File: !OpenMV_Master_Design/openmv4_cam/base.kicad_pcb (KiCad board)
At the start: 4 copper layers, 129.6 x 57.7 mm, 58 parts, among them J5 XF2M-1015-1A, Q1 BSS138, Q2 Si2301BDS, U1 STM32H743VIT6, U2 OV7725, U5 TPS731XX, U8 PAM2305AABADJ, X1 MF-CON-MICROUSB-RIGHT, X2 USD-1040310811, Y1 7S-12.000MAHE-T

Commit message: Moved SD card
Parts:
- moved X2 16.6 mm to (149.5, 90.3), turned to 0 degrees
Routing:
- net /SDIO_CMD: track 22.1 -> 11.1 mm
- net /SDIO_CLK: track 16.4 -> 6.95 mm
- net /SDIO_D3: track 18.3 -> 11.0 mm
- net /SDIO_D2: track 17.4 -> 11.8 mm
- net GND: track 75.9 -> 72.8 mm, vias 36 -> 35
- net VCC: vias 32 -> 30
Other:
- board size 129.6 x 57.7 mm -> 35.8 x 44.4 mm
- board text removed: "3.3V"
- board text removed: "BOOT"
- board text removed: "Built by MacroFab"
- board text removed: "LED1=Red"
- board text removed: "LED2=Green"
- board text removed: "LED3=Blue"
- board text removed: "LED4=IR"
- board text removed: "Made in USA"
- board text removed: "P0"
- board text removed: "P1"
- board text removed: "P2"
- board text removed: "P3"
- board text removed: "P4"
- board text removed: "P5"
- board text removed: "P6"
- board text removed: "P7"
- board text removed: "P8"
- board text removed: "P9"
- board text removed: "SYN"
- board text removed: "VIN"
- board text removed: "v00"

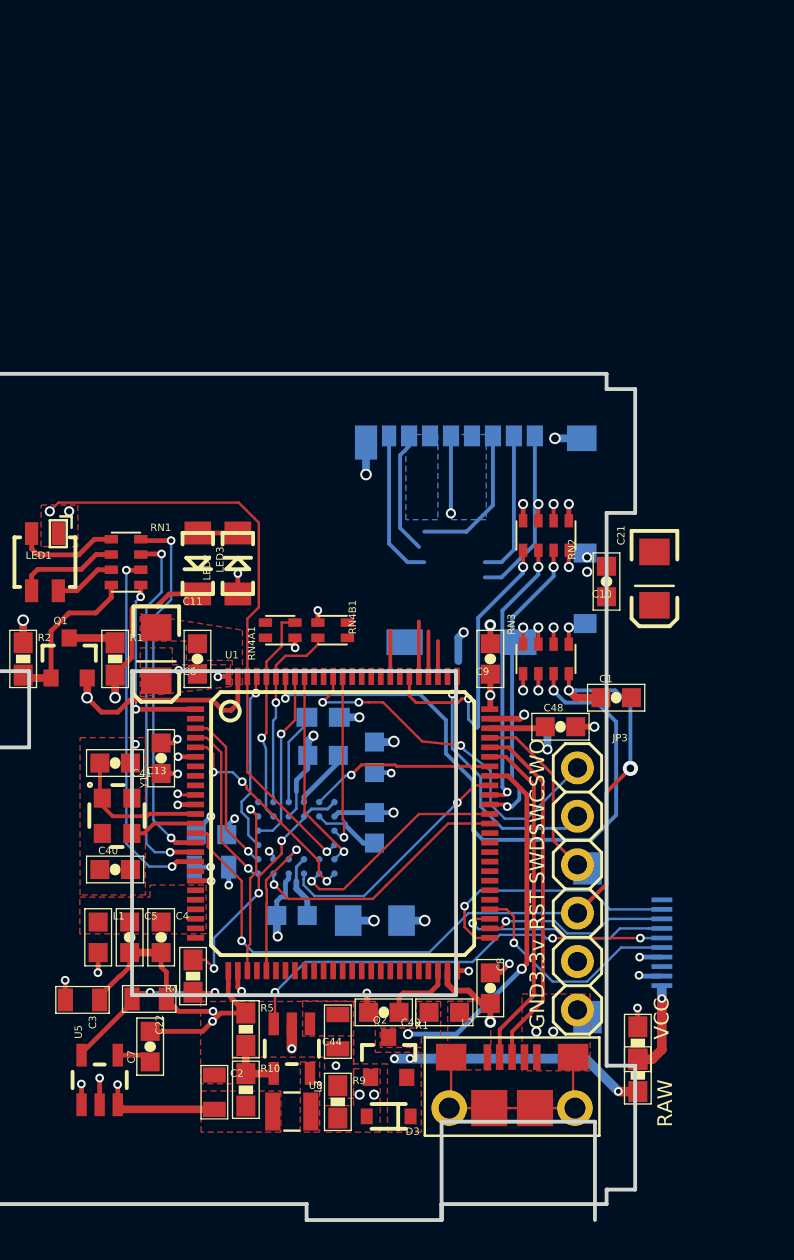
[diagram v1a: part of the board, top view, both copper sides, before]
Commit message: Move USB to cam side, more SD card changes
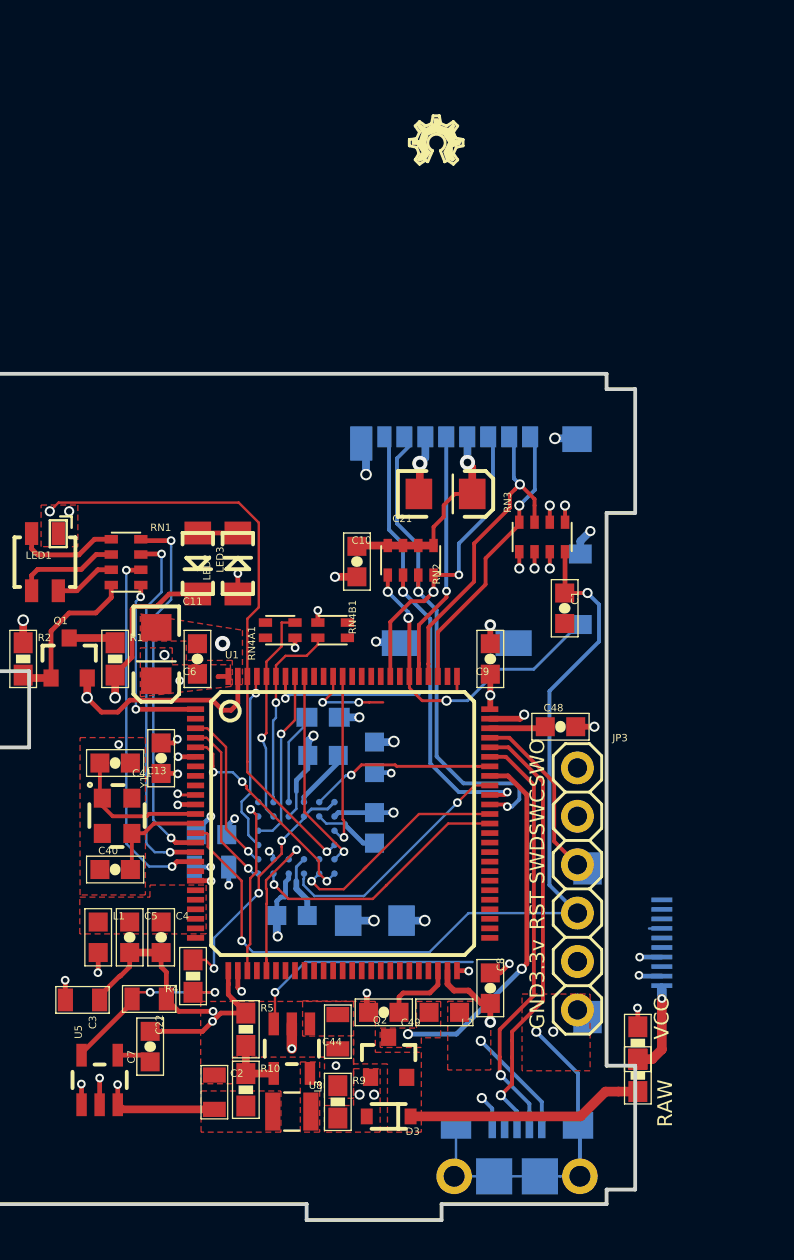
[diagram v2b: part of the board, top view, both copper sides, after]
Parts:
- added LOGO1: OSHW_LOGO_FILLX0100-NT, base:OSHW_FILLX100_NOTEXT, F.Cu at (152.0, 76.2)
- J5: footprint XF2M-1015-1A:XF2M-1015-1A -> base:XF2M-1015-1A
- X1: moved to B.Cu
- moved C10 13.1 mm to (149.2, 97.1), turned to 270 degrees
- moved C21 11.8 mm to (153.9, 93.5), turned to 0 degrees
- moved RN2 7.22 mm to (152.1, 97.0)
- moved RN3 6.40 mm to (159.0, 95.8)
- moved C1 5.41 mm to (160.2, 99.5), turned to 270 degrees
- moved X1 3.59 mm to (157.7, 128.0), turned to 180 degrees
- moved X2 0.25 mm to (149.2, 90.3)
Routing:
- net /BOOT0: track 34.6 -> 9.16 mm
- net /SPI3_SCLK/TRACESWO: track 19.5 -> 4.76 mm, vias 3 -> 2
- net /SPI2_NSS: track 13.8 -> 0.00 mm, vias 1 -> 0
- net /SWCLK: track 13.4 -> 0.67 mm, vias 1 -> 0
- net /SPI2_MOSI: track 12.1 -> 0.00 mm, vias 1 -> 0
- net /SPI2_MISO: track 11.5 -> 0.68 mm, vias 1 -> 0
- net /PWR_EN: track 23.3 -> 12.7 mm, vias 3 -> 1
- net /SPI2_SCLK: track 9.83 -> 0.00 mm, vias 1 -> 0
- net VCC: track 32.0 -> 39.7 mm, vias 30 -> 27
- net /SDIO_CLK: track 6.95 -> 13.2 mm
- net GND: track 72.8 -> 78.9 mm, vias 35 -> 36
- net /SDIO_D3: track 11.0 -> 17.0 mm
- net Net-(X1-PadS1): track 12.0 -> 17.9 mm, vias 0 -> 1
- net Net-(L2-Pad1): track 0.00 -> 5.76 mm, vias 0 -> 1
- net /SDIO_CMD: track 11.1 -> 16.2 mm, vias 1 -> 2
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- removed copper zone on B.Cu, net GND
- removed copper zone on B.Cu, net VCC
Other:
- outline, holes or cut-outs redrawn

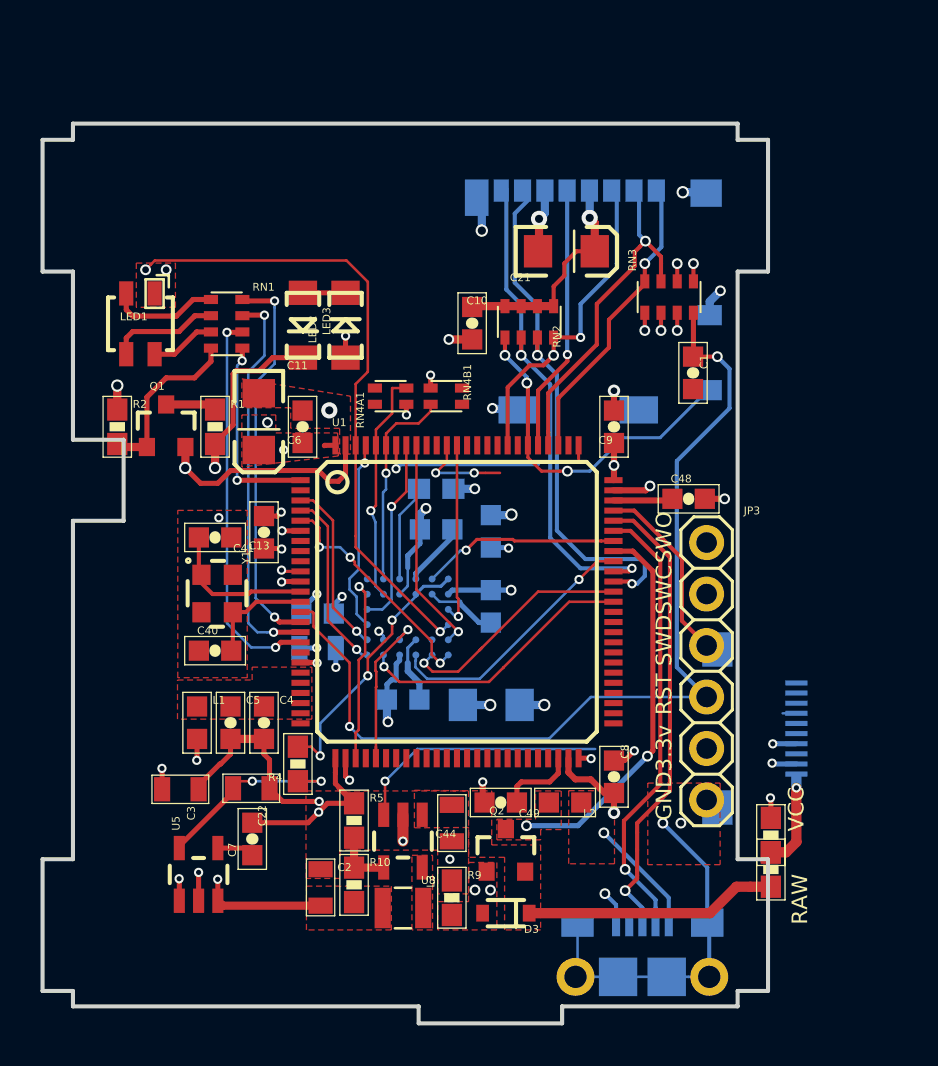
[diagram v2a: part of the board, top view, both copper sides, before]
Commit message: Fixed connections to debug headers
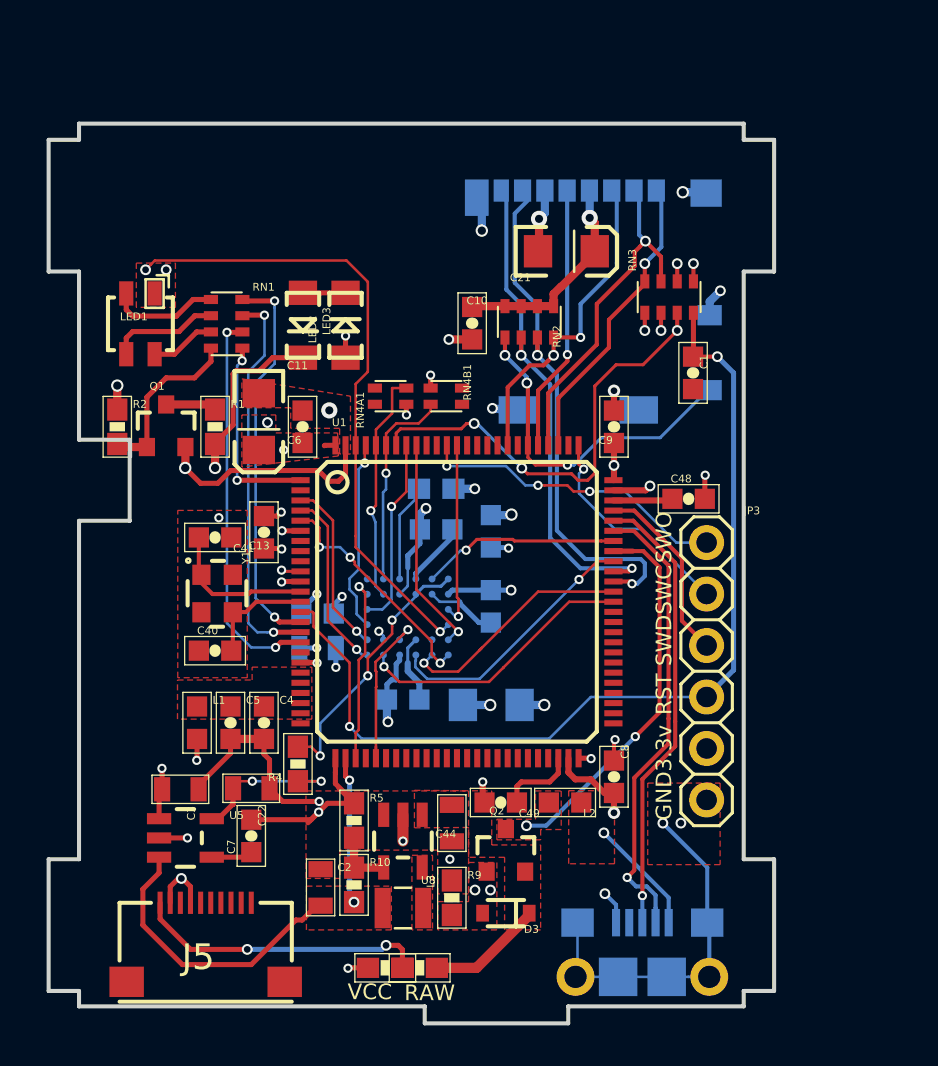
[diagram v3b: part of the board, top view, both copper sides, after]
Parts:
- J5: moved to F.Cu
- moved J5 30.4 mm to (136.1, 125.7), turned to 0 degrees
- moved R7 20.1 mm to (145.0, 128.9), turned to 0 degrees
- moved R6 18.0 mm to (146.7, 128.9), turned to 0 degrees
- moved U5 1.91 mm to (135.1, 122.5), turned to 270 degrees
- moved C7 0.16 mm to (138.3, 122.4)
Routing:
- net VCC: track 39.7 -> 53.8 mm, vias 27 -> 26
- net /BOOT0: track 9.16 -> 22.3 mm, vias 2 -> 3
- net /PWR_EN: track 12.7 -> 0.09 mm, vias 1 -> 0
- net /SPI3_SCLK/TRACESWO: track 4.76 -> 15.4 mm, vias 2 -> 3
- net /SWCLK: track 0.67 -> 10.9 mm, vias 0 -> 1
- net Net-(J5-Pad1): track 4.69 -> 14.5 mm, vias 1 -> 2
- net RAW: track 12.5 -> 5.73 mm
- net VDDA: track 9.69 -> 7.99 mm
- net GND: track 78.9 -> 80.3 mm, vias 36 -> 35
- net /NRST: track 47.9 -> 46.9 mm
- net /SPI2_MISO: track 0.68 -> 0.00 mm
- net /FS_DM: track 22.2 -> 22.8 mm

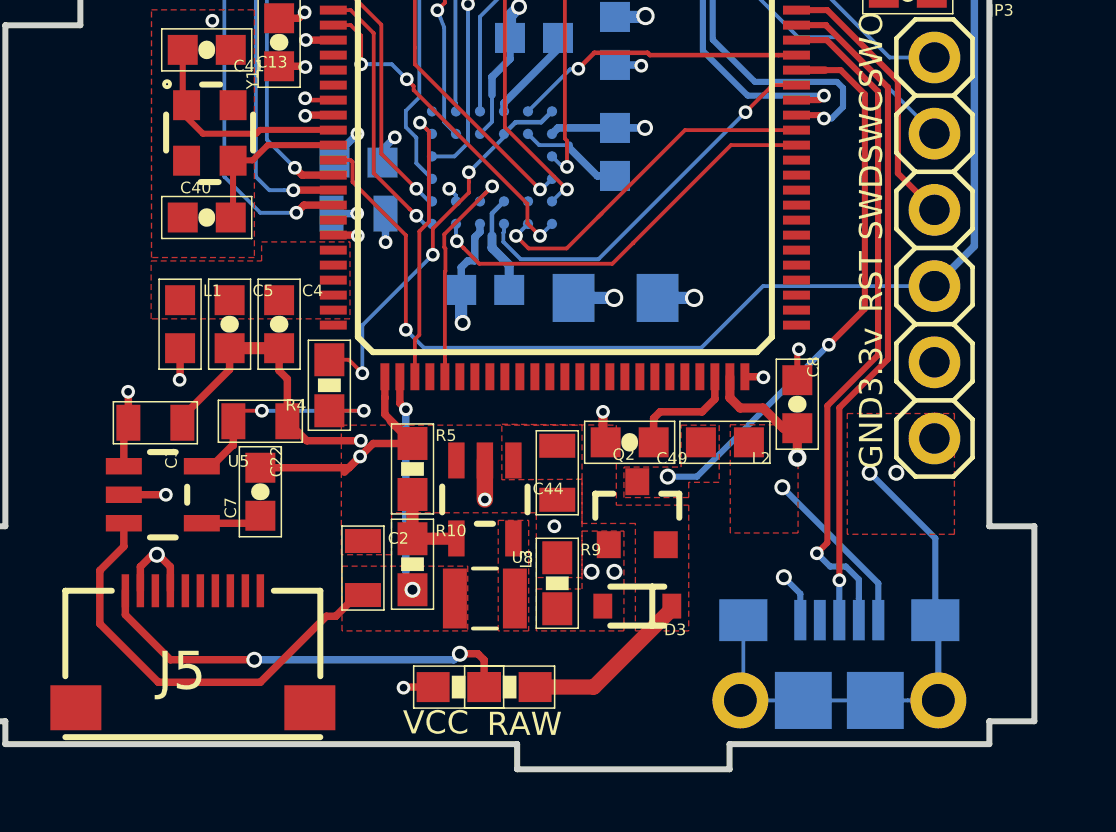
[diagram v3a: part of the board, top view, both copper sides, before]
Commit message: flat flex moved
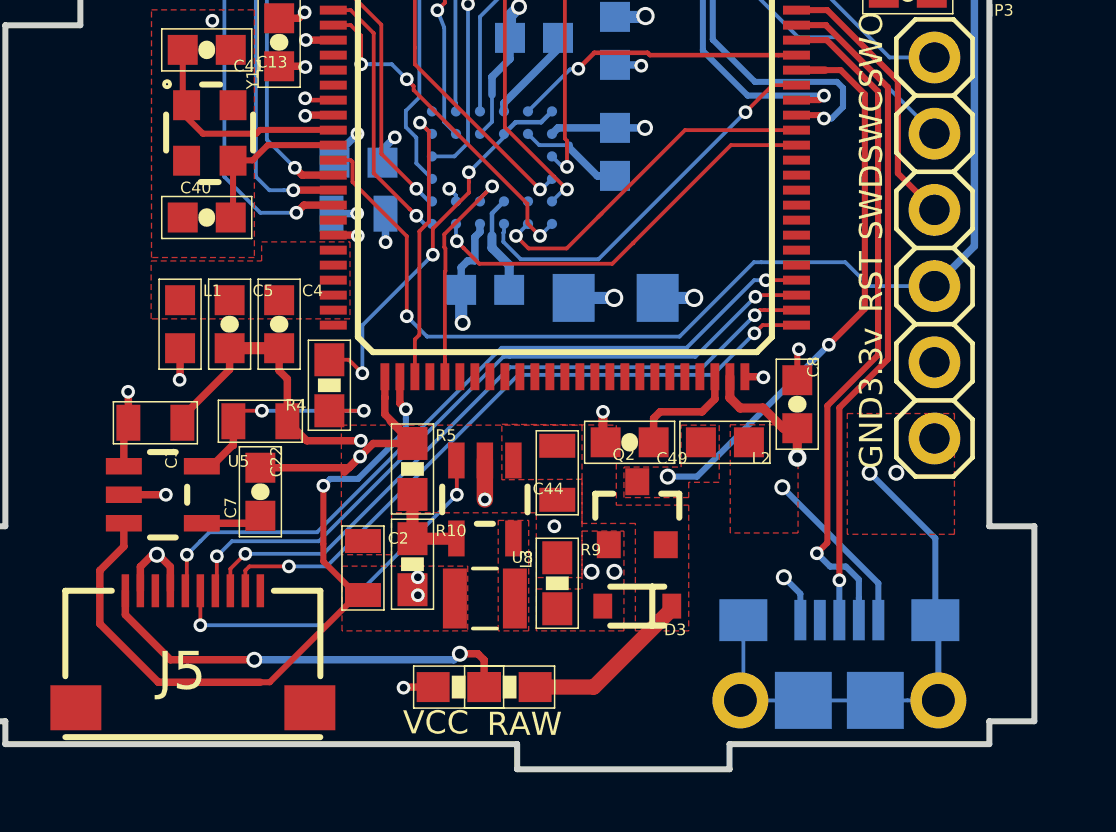
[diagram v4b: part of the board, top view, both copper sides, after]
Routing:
- net /SPI2_MOSI: track 0.00 -> 25.3 mm, vias 0 -> 2
- net /SPI2_MISO: track 0.00 -> 24.1 mm, vias 0 -> 2
- net /SPI2_SCLK: track 0.00 -> 23.2 mm, vias 0 -> 2
- net /SPI2_NSS: track 0.00 -> 22.4 mm, vias 0 -> 2
- net /PWR_EN: track 0.09 -> 12.7 mm, vias 0 -> 2
- net VCC: track 53.8 -> 56.0 mm, vias 26 -> 28

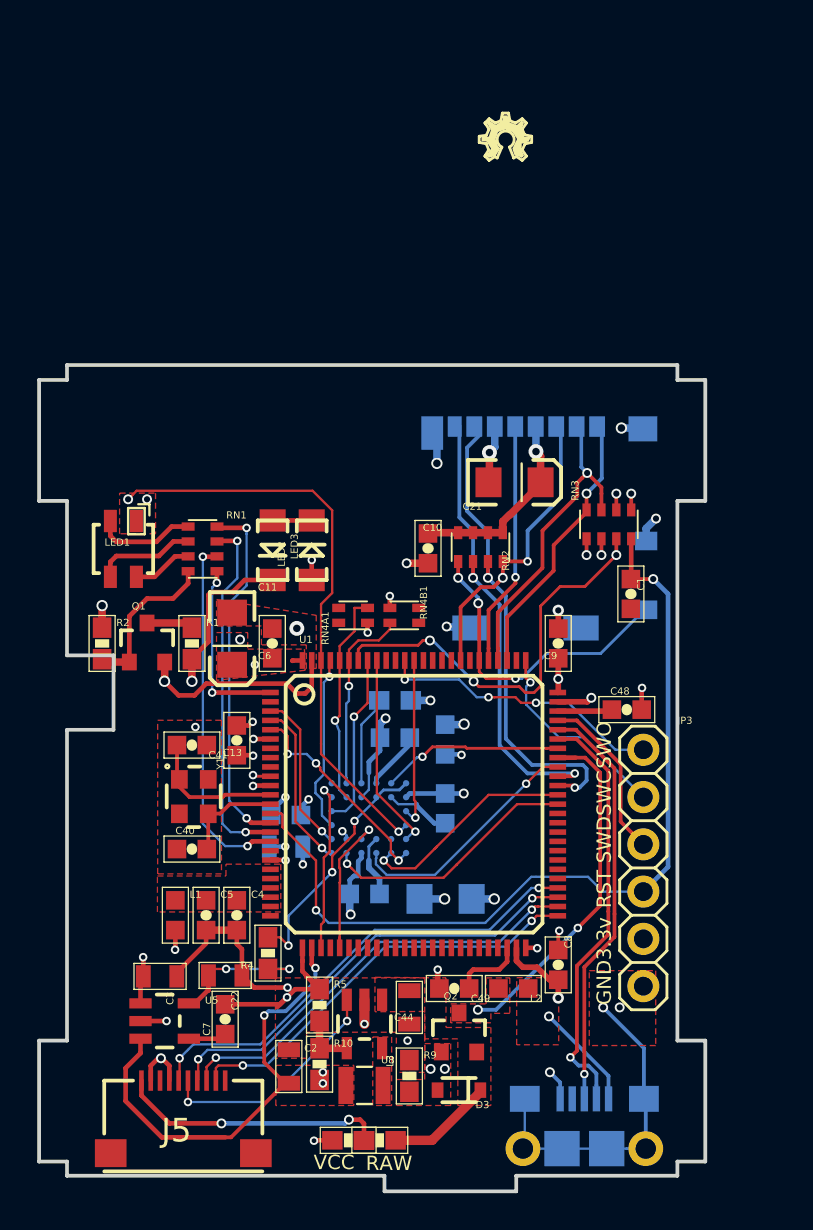
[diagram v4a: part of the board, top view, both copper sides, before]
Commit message: Fixed Silk
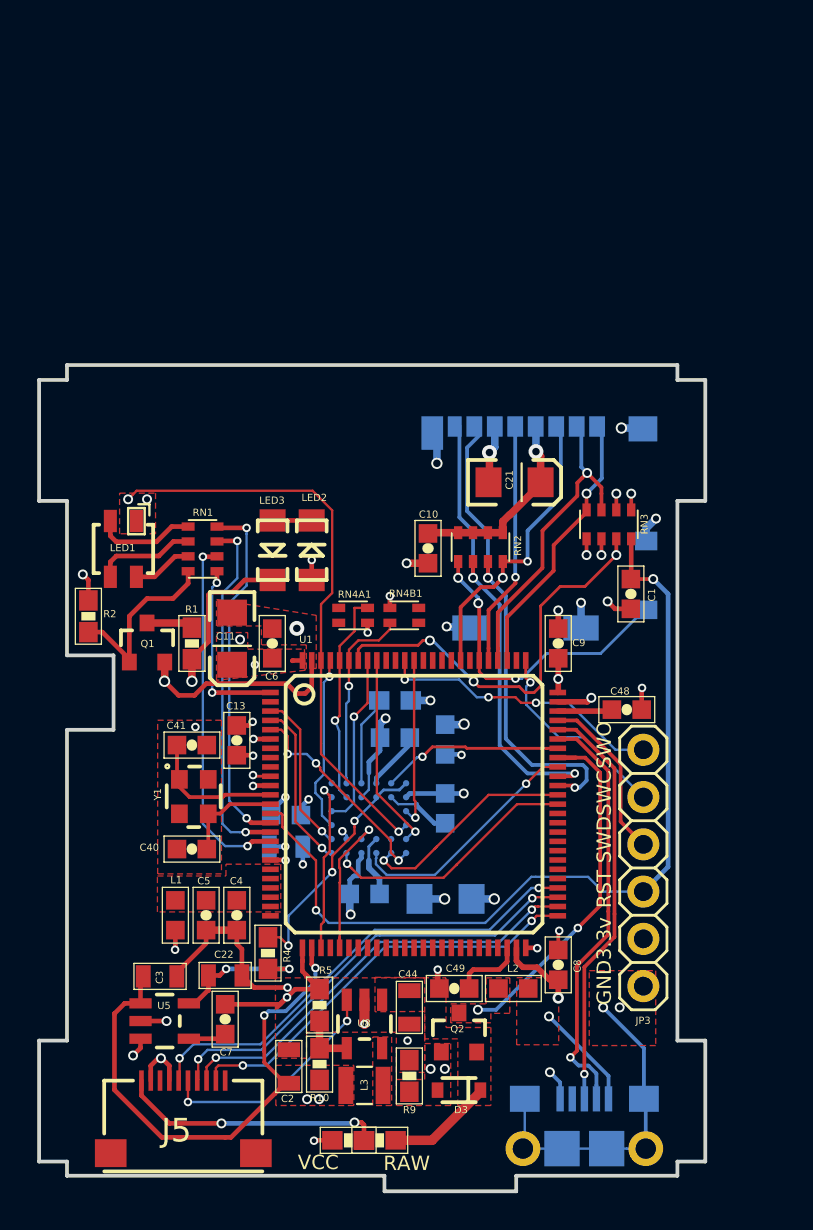
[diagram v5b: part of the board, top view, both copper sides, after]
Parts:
- removed LOGO1: OSHW_LOGO_FILLX0100-NT, base:OSHW_FILLX100_NOTEXT
- moved R2 1.64 mm to (131.0, 100.8)
- renumbered X1 to USB
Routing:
- net GND: track 80.3 -> 83.4 mm, vias 35 -> 37
- net VCC: track 56.0 -> 58.9 mm
- net Net-(Q1-Pad1): track 8.53 -> 9.97 mm
